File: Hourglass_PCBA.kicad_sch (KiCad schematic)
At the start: 0 parts

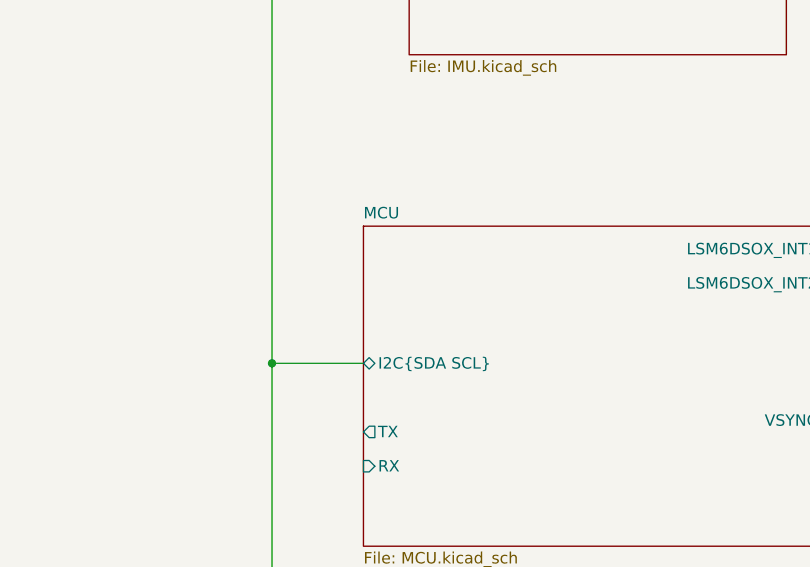
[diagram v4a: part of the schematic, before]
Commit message: Completed schematic for MCU section
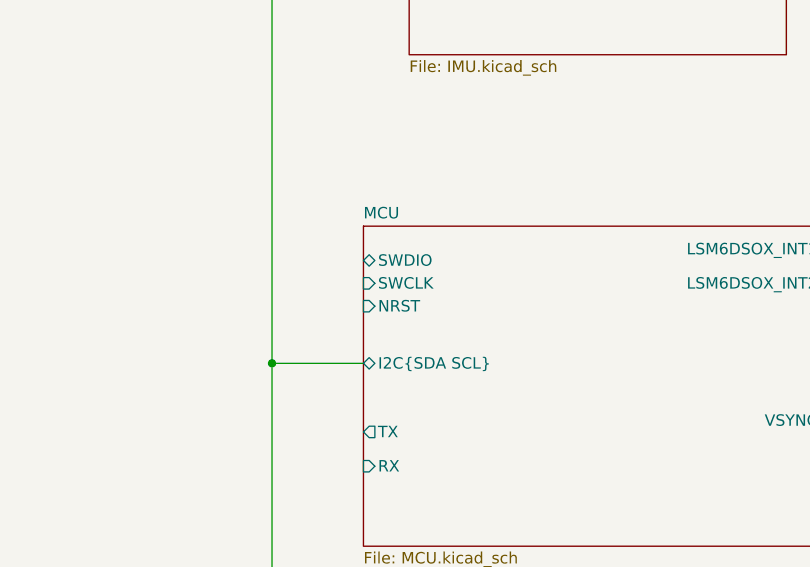
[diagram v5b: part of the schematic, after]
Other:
- sheet MCU ports: added NRST, SWCLK, SWDIO; removed none
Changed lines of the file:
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@@
+			)
+		)
+		(pin "NRST" input
+			(at 124.46 77.47 180)
+			(effects
+				(font
+					(size 1.27 1.27)
+				)
+				(justify left)
+			)
+		)
+		(pin "SWCLK" input
+			(at 124.46 74.93 180)
+			(effects
+				(font
+					(size 1.27 1.27)
+				)
+				(justify left)
+			)
+		)
+		(pin "SWDIO" bidirectional
+			(at 124.46 72.39 180)
+			(effects
+				(font
+					(size 1.27 1.27)
+				)
+				(justify left)
 			)
 		)

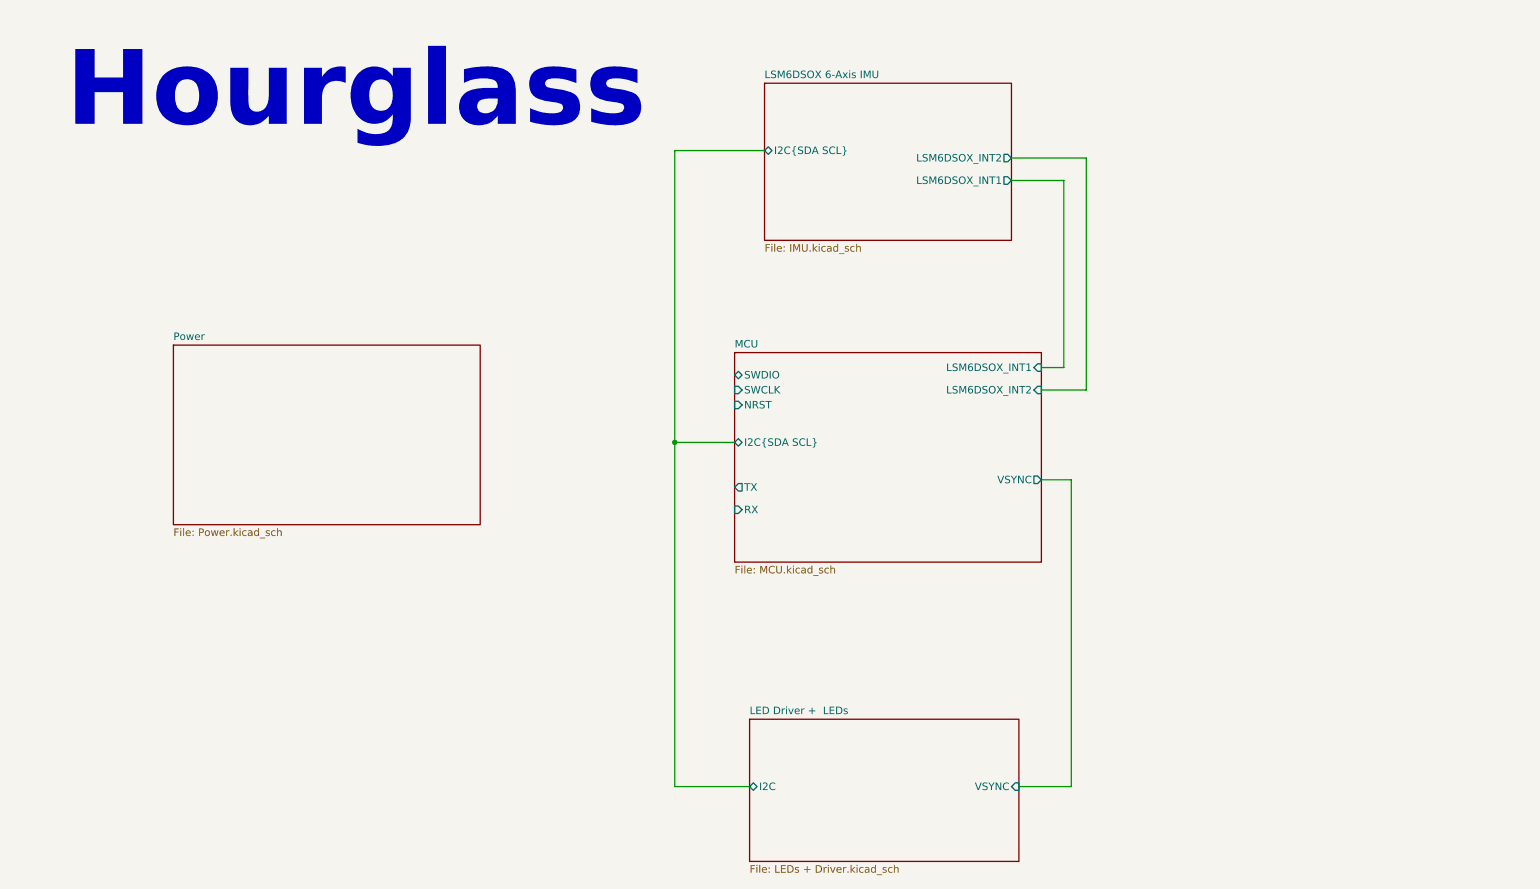
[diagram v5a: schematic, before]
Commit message: First complete schematic with TPs.
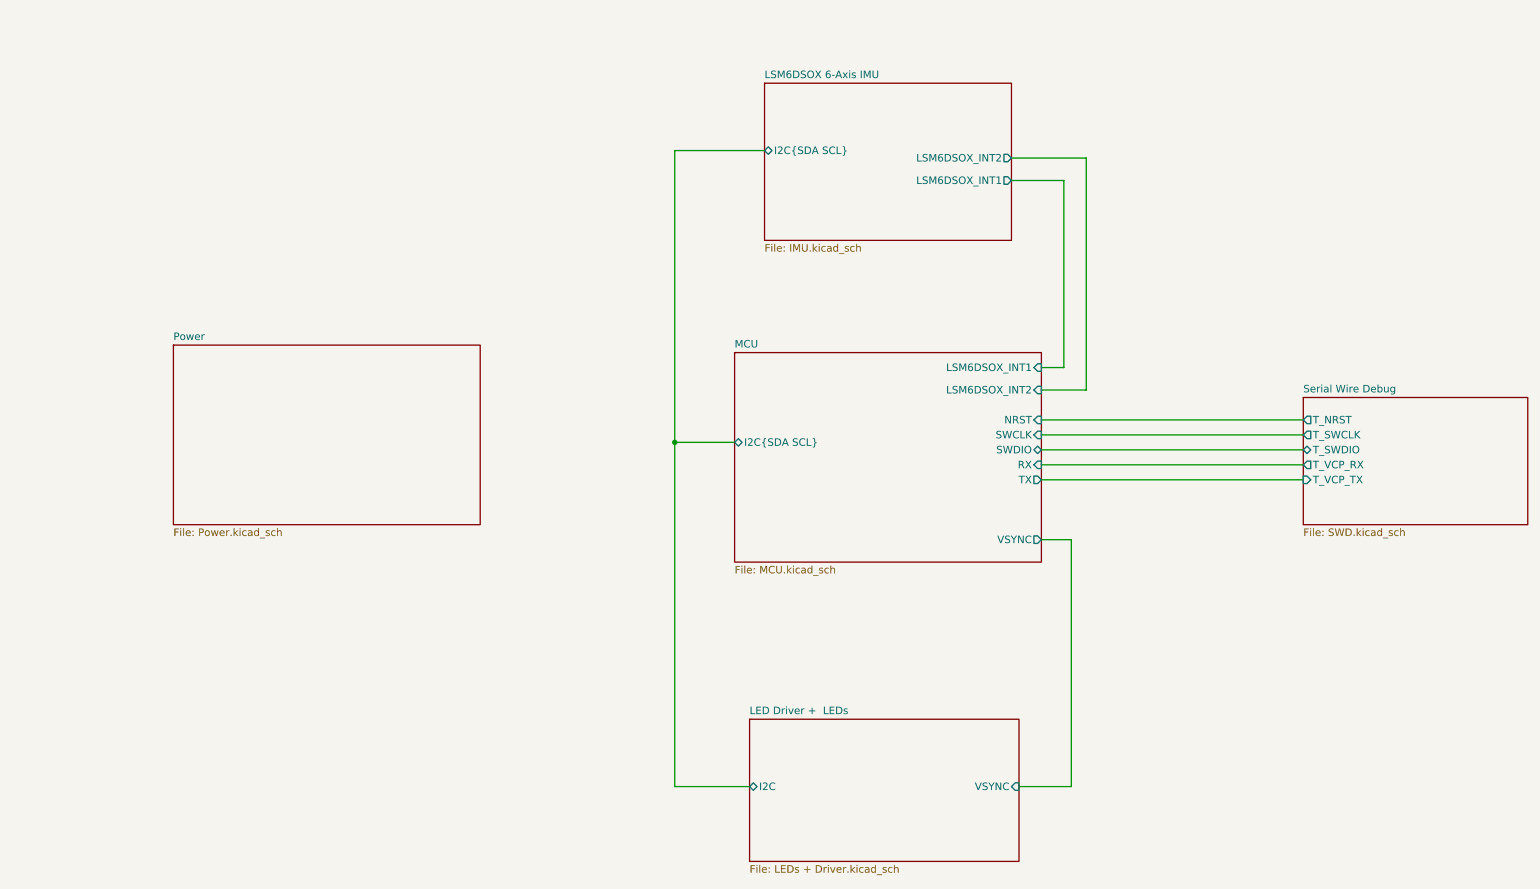
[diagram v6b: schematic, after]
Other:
- added sheet Serial Wire Debug (SWD.kicad_sch)
- note removed: "Hourglass"

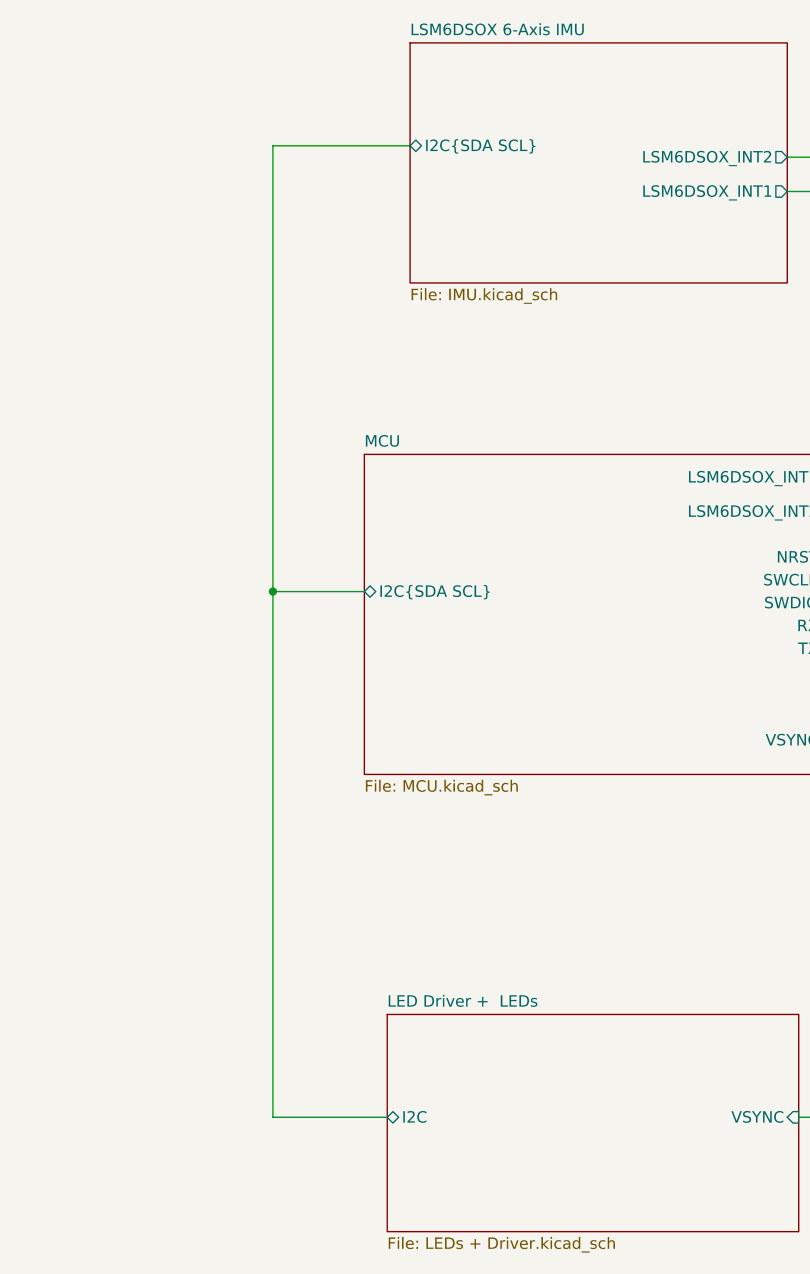
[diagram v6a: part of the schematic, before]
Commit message: Addressed DRC warnings and errors.
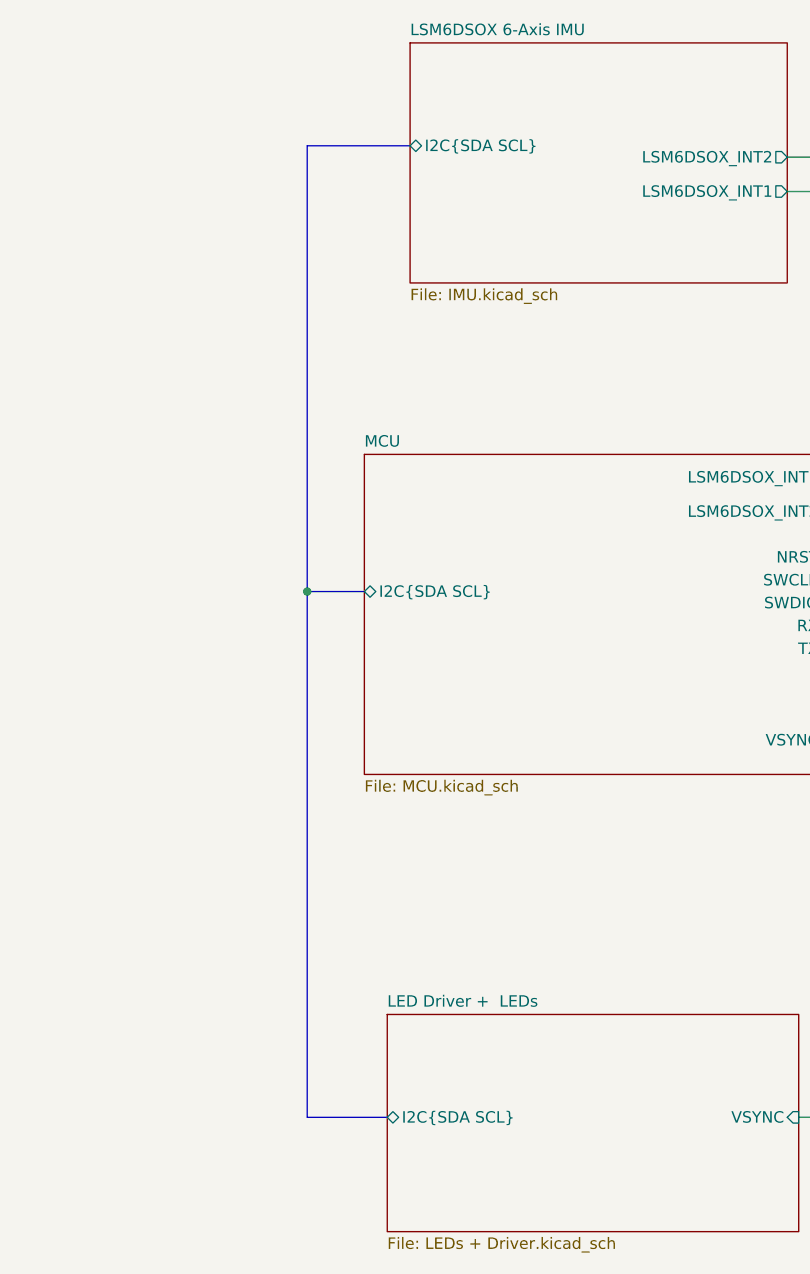
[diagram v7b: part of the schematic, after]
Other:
- sheet LED Driver +  LEDs ports: added I2C{SDA SCL}; removed I2C
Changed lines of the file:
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@@
 	)
 	(junction
-		(at 114.3 83.82)
+		(at 118.11 83.82)
 		(diameter 0)
 		(color 0 0 0 0)
 	)
-	(wire
+	(bus
 		(pts
-			(xy 181.61 142.24) (xy 172.72 142.24)
+			(xy 118.11 142.24) (xy 127 142.24)
 		)
 		(stroke
@@
 		)
 	)
-	(wire
+	(bus
 		(pts
-			(xy 176.53 82.55) (xy 220.98 82.55)
+			(xy 118.11 34.29) (xy 118.11 83.82)
 		)
 		(stroke
@@
 	(wire
 		(pts
-			(xy 184.15 35.56) (xy 184.15 74.93)
+			(xy 181.61 142.24) (xy 172.72 142.24)
 		)
 		(stroke
@@
 	(wire
 		(pts
-			(xy 176.53 80.01) (xy 220.98 80.01)
+			(xy 176.53 82.55) (xy 220.98 82.55)
 		)
 		(stroke
@@
 		)
 	)
-	(wire
+	(bus
 		(pts
-			(xy 176.53 87.63) (xy 220.98 87.63)
+			(xy 118.11 83.82) (xy 118.11 142.24)
 		)
 		(stroke
@@
 	(wire
 		(pts
-			(xy 180.34 39.37) (xy 180.34 71.12)
+			(xy 184.15 35.56) (xy 184.15 74.93)
 		)
 		(stroke
@@
 	(wire
 		(pts
-			(xy 176.53 90.17) (xy 220.98 90.17)
+			(xy 176.53 80.01) (xy 220.98 80.01)
 		)
 		(stroke
@@
 	(wire
 		(pts
-			(xy 176.53 100.33) (xy 181.61 100.33)
+			(xy 176.53 87.63) (xy 220.98 87.63)
 		)
 		(stroke
@@
 	(wire
 		(pts
-			(xy 114.3 142.24) (xy 114.3 83.82)
+			(xy 180.34 39.37) (xy 180.34 71.12)
 		)
 		(stroke
@@
 	(wire
 		(pts
-			(xy 124.46 83.82) (xy 114.3 83.82)
+			(xy 176.53 90.17) (xy 220.98 90.17)
 		)
 		(stroke
@@
 	(wire
 		(pts
-			(xy 127 142.24) (xy 114.3 142.24)
+			(xy 176.53 100.33) (xy 181.61 100.33)
 		)
 		(stroke
@@
 		)
 	)
-	(wire
+	(bus
 		(pts
-			(xy 171.45 39.37) (xy 180.34 39.37)
+			(xy 129.54 34.29) (xy 118.11 34.29)
 		)
 		(stroke
@@
 		)
 	)
-	(wire
+	(bus
 		(pts
-			(xy 114.3 83.82) (xy 114.3 34.29)
+			(xy 118.11 83.82) (xy 124.46 83.82)
 		)
 		(stroke
@@
 	(wire
 		(pts
-			(xy 184.15 74.93) (xy 176.53 74.93)
+			(xy 171.45 39.37) (xy 180.34 39.37)
 		)
 		(stroke
@@
 	(wire
 		(pts
-			(xy 171.45 35.56) (xy 184.15 35.56)
+			(xy 184.15 74.93) (xy 176.53 74.93)
 		)
 		(stroke
@@
 	(wire
 		(pts
-			(xy 180.34 71.12) (xy 176.53 71.12)
+			(xy 171.45 35.56) (xy 184.15 35.56)
 		)
 		(stroke
@@
 	(wire
 		(pts
-			(xy 114.3 34.29) (xy 129.54 34.29)
+			(xy 180.34 71.12) (xy 176.53 71.12)
 		)
 		(stroke
@@
 			"AAAAAAAAAAAAAAAAAAAAAAAAAAAAAAAAAAAAAAAAAAAAAAAAAAAAAAAAAAAAAAAAAAAAAAAAAAAA"
 			"AAAAAAAAAAAAAAAAAAAAAAAAAAAAAAAAAAAAAAAAAAAAAAAAAAAAAAAAAAAAAAAAAAAAAAAAAAAA"
+			"AAAAAAAAAAAAAAAAAAAAAAAAAAAAAAAAAAAAAAAAAAAAAAAAAAAAAAAAAAAAAAAAAAAAAAAAAAAA"
+			"AAAAAAAAAAAAAAAAAAAAAAAAAAAAAAAAAAAAAAAAAAAAAAAAAAAAAAAAAAAAAAAAAAAAAAAAAAAA"
+			"AAAAAAAAAAAAAAAAAAAAAAAAAAAAAAAAAAAAAAAAAAAAAAAAAAAAAAAAAAAAAAAAAAAAAAAAAAAA"
+			"AAAAAAAAAAAAAAAAAAAAAAAAAAAAAAAAAAAAAAAAAAAAAAAAAAAAAAAAAAAAAAAAAAAAAAAAAAAA"
+			"AAAAAAAAAAAAAAAAAAAAAAAAAAAAAAAAAAAAAAAAAAAAAAAAAAAAAAAAAAAAAAAAAAAAAAAAAAAA"
+			"AAAAAAAAAAAAAAAAAAAAAAAAAAAAAAAAAAAAAAAAAAAAAAAAAAAAAAAAAAAAAAAAAAAAAAAAAAAA"
+			"AAAAAAAAAAAAAAAAAAAAAAAAAAAAAAAAAAAAAAAAAAAAAAAAAAAAAAAAAAAAAAAAAAAAAAAAAAAA"
+			"AAAAAAAAAAAAAAAAAAAAAAAAAAAAAAAAAAAAAAAAAAAAAAAAAAAAAAAAAAAAAAAAAAAAAAAAAAAA"
+			"AAAAAAAAAAAAAAAAAAAAAAAAAAAAAAAAAAAAAAAAAAAAAAAAAAAAAAAAAAAAAAAAAAAAAAAAAAAA"
+			"AAAAAAAAAAAAAAAAAAAAAAAAAAAAAAAAAAAAAAAAAAAAAAAAAAAAAAAAAAAAAAAAAAAAAAAAAAAA"
+			"AAAAAAAAAAAAAAAAAAAAAAAAAAAAAAAAAAAAAAAAAAAAAAAAAAAAAAAAAAAAAAAAAAAAAAAAAAAA"
+			"AAAAAAAAAAAAAAAAAAAAAAAAAAAAAAAAAAAAAAAAAAAAAAAAAAAAAAAAAAAAAAAAAAAAAAAAAAAA"
+			"AAAAAAAAAAAAAAAAAAAAAAAAAAAAAAAAAAAAAAAAAAAAAAAAAAAAAAAAAAAAAAAAAAAAAAAAAAAA"
+			"AAAAAAAAAAAAAAAAAAAAAAAAAAAAAAAAAAAAAAAAAAAAAAAAAAAAAAAAAAAAAAAAAAAAAAAAAAAA"
+			"AAAAAAAAAAAAAAAAAAAAAAAAAAAAAAAAAAAAAAAAAAAAAAAAAAAAAAAAAAAAAAAAAAAAAAAAAAAA"
+			"AAAAAAAAAAAAAAAAAAAAAAAAAAAAAAAAAAAAAAAAAAAAAAAAAAAAAAAAAAAAAAAAAAAAAAAAAAAA"
+			"AAAAAAAAAAAAAAAAAAAAAAAAAAAAAAAAAAAAAAAAAAAAAAAAAAAAAAAAAAAAAAAAAAAAAAAAAAAA"
+			"AAAAAAAAAAAAAAAAAAAAAAAAAAAAAAAAAAAAAAAAAAAAAAAAAAAAAAAAAAAAAAAAAAAAAAAAAAAA"
+			"AAAAAAAAAAAAAAAAAAAAAAAAAAAAAAAAAAAAAAAAAAAAAAAAAAAAAAAAAAAAAAAAAAAAAAAAAAAA"
+			"AAAAAAAAAAAAAAAAAAAAAAAAAAAAAAAAAAAAAAAAAAAAAAAAAAAAAAAAAAAAAAAAAAAAAAAAAAAA"
+			"AAAAAAAAAAAAAAAAAAAAAAAAAAAAAAAAAAAAAAAAAAAAAAAAAAAAAAAAAAAAAAAAAAAAAAAAAAAA"
+			"AAAAAAAAAAAAAAAAAAAAAAAAAAAAAAAAAAAAAAAAAAAAAAAAAAAAAAAAAAAAAAAAAAAAAAAAAAAA"
+			"AAAAAAAAAAAAAAAAAAAAAAAAAAAAAAAAAAAAAAAAAAAAAAAAAAAAAAAAAAAAAAAAAAAAAAAAAAAA"
+			"AAAAAAAAAAAAAAAAAAAAAAAAAAAAAAAAAAAAAAAAAAAAAAAAAAAAAAAAAAAAAAAAAAAAAAAAAAAA"
+			"AAAAAAAAAAAAAAAAAAAAAAAAAAAAAAAAAAAAAAAAAAAAAAAAAAAAAAAAAAAAAAAAAAAAAAAAAAAA"
+			"AAAAAAAAAAAAAAAAAAAAAAAAAAAAAAAAAAAAAAAAAAAAAAAAAAAAAAAAAAAAAAAAAAAAAAAAAAAA"
+			"AAAAAAAAAAAAAAAAAAAAAAAAAAAAAAAAAAAAAAAAAAAAAAAAAAAAAAAAAAAAAAAAAAAAAAAAAAAA"
+			"AAAAAAAAAAAAAAAAAAAAAAAAAAAAAAAAAAAAAAAAAAAAAAAAAAAAAAAAAAAAAAAAAAAAAAAAAAAA"
+			"AAAAAAAAAAAAAAAAAAAAAAAAAAAAAAAAAAAAAAAAAAAAAAAAAAAAAAAAAAAAAAAAAAAAAAAAAAAA"
+			"AAAAAAAAAAAAAAAAAAAAAAAAAAAAAAAAAAAAAAAAAAAAAAAAAAAAAAAAAAAAAAAAAAAAAAAAAAAA"
+			"AAAAAAAAAAAAAAAAAAAAAAAAAAAAAAAAAAAAAAAAAAAAAAAAAAAAAAAAAAAAAAAAAAAAAAAAAAAA"
+			"AAAAAAAAAAAAAAAAAAAAAAAAAAAAAAAAAAAAAAAAAAAAAAAAAAAAAAAAAAAAAAAAAAAAAAAAAAAA"
+			"AAAAAAAAAAAAAAAAAAAAAAAAAAAAAAAAAAAAAAAAAAAAAAAAAAAAAAAAAAAAAAAAAAAAAAAAAAAA"
+			"AAAAAAAAAAAAAAAAAAAAAAAAAAAAAAAAAAAAAAAAAAAAAAAAAAAAAAAAAAAAAAAAAAAAAAAAAAAA"
+			"AAAAAAAAAAAAAAAAAAAAAAAAAAAAAAAAAAAAAAAAAAAAAAAAAAAAAAAAAAAAAAAAAAAAAAAAAAAA"
+			"AAAAAAAAAAAAAAAAAAAAAAAAAAAAAAAAAAAAAAAAAAAAAAAAAAAAAAAAAAAAAAAAAAAAAAAAAAAA"
+			"AAAAAAAAAAAAAAAAAAAAAAAAAAAAAAAAAAAAAAAAAAAAAAAAAAAAAAAAAAAAAAAAAAAAAAAAAAAA"
+			"AAAAAAAAAAAAAAAAAAAAAAAAAAAAAAAAAAAAAAAAAAAAAAAAAAAAAAAAAAAAAAAAAAAAAAAAAAAA"
+			"AAAAAAAAAAAAAAAAAAAAAAAAAAAAAAAAAAAAAAAAAAAAAAAAAAAAAAAAAAAAAAAAAAAAAAAAAAAA"
+			"AAAAAAAAAAAAAAAAAAAAAAAAAAAAAAAAAAAAAAAAAAAAAAAAAAAAAAAAAAAAAAAAAAAAAAAAAAAA"
+			"AAAAAAAAAAAAAAAAAAAAAAAAAAAAAAAAAAAAAAAAAAAAAAAAAAAAAAAAAAAAAAAAAAAAAAAAAAAA"
+			"AAAAAAAAAAAAAAAAAAAAAAAAAAAAAAAAAAAAAAAAAAAAAAAAAAAAAAAAAAAAAAAAAAAAAAAAAAAA"
+			"AAAAAAAAAAAAAAAAAAAAAAAAAAAAAAAAAAAAAAAAAAAAAAAAAAAAAAAAAAAAAAAAAAAAAAAAAAAA"
+			"AAAAAAAAAAAAAAAAAAAAAAAAAAAAAAAAAAAAAAAAAAAAAAAAAAAAAAAAAAAAAAAAAAAAAAAAAAAA"
+			"AAAAAAAAAAAAAAAAAAAAAAAAAAAAAAAAAAAAAAAAAAAAAAAAAAAAAAAAAAAAAAAAAAAAAAAAAAAA"
+			"AAAAAAAAAAAAAAAAAAAAAAAAAAAAAAAAAAAAAAAAAAAAAAAAAAAAAAAAAAAAAAAAAAAAAAAAAAAA"
+			"AAAAAAAAAAAAAAAAAAAAAAAAAAAAAAAAAAAAAAAAAAAAAAAAAAAAAAAAAAAAAAAAAAAAAAAAAAAA"
+			"AAAAAAAAAAAAAAAAAAAAAAAAAAAAAAAAAAAAAAAAAAAAAAAAAAAAAAAAAAAAAAAAAAAAAAAAAAAA"
+			"AAAAAAAAAAAAAAAAAAAAAAAAAAAAAAAAAAAAAAAAAAAAAAAAAAAAAAAAAAAAAAAAAAAAAAAAAAAA"
+			"AAAAAAAAAAAAAAAAAAAAAAAAAAAAAAAAAAAAAAAAAAAAAAAAAAAAAAAAAAAAAAAAAAAAAAAAAAAA"
+			"AAAAAAAAAAAAAAAAAAAAAAAAAAAAAAAAAAAAAAAAAAAAAAAAAAAAAAAAAAAAAAAAAAAAAAAAAAAA"
+			"AAAAAAAAAAAAAAAAAAAAAAAAAAAAAAAAAAAAAAAAAAAAAAAAAAAAAAAAAAAAAAAAAAAAAAAAAAAA"
+			"AAAAAAAAAAAAAAAAAAAAAAAAAAAAAAAAAAAAAAAAAAAAAAAAAAAAAAAAAAAAAAAAAAAAAAAAAAAA"
+			"AAAAAAAAAAAAAAAAAAAAAAAAAAAAAAAAAAAAAAAAAAAAAAAAAAAAAAAAAAAAAAAAAAAAAAAAAAAA"
 			"AAAAAAAAAAAAAAAAAAAAAAAAAAAAAAAAAAAAAAAAAA=="
 		)
@@
 			)
 		)
-		(pin "I2C" bidirectional
+		(pin "I2C{SDA SCL}" bidirectional
 			(at 127 142.24 180)
 			(effects
